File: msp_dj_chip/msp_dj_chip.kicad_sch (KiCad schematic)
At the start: 87 parts, among them J1 Conn_01x04_Pin, J10 Conn_01x02_Socket, J11 Conn_01x02_Socket, J12 Conn_01x02_Socket, J13 Conn_01x02_Socket, J14 Conn_01x02_Socket, J15 Conn_01x02_Socket, J16 Conn_01x02_Socket, J17 Conn_01x02_Socket, J18 Conn_01x02_Socket, J19 Conn_01x02_Socket, J2 Conn_01x04_Pin, J20 Conn_01x02_Socket, J21 Conn_01x02_Socket, J22 Conn_01x06_Socket, J23 Conn_01x06_Socket, J3 Conn_01x02_Socket, J4 Conn_01x02_Socket, J5 Conn_01x02_Socket, J6 Conn_01x02_Socket, J8 Conn_02x05_Odd_Even, J9 Conn_01x02_Socket, SW1 SW_MEC_5E, U2 DAC60502, U4 NCP1117-3.3_SOT223, U8 NCV272DMR2G, Y2 Crystal_GND24_Small

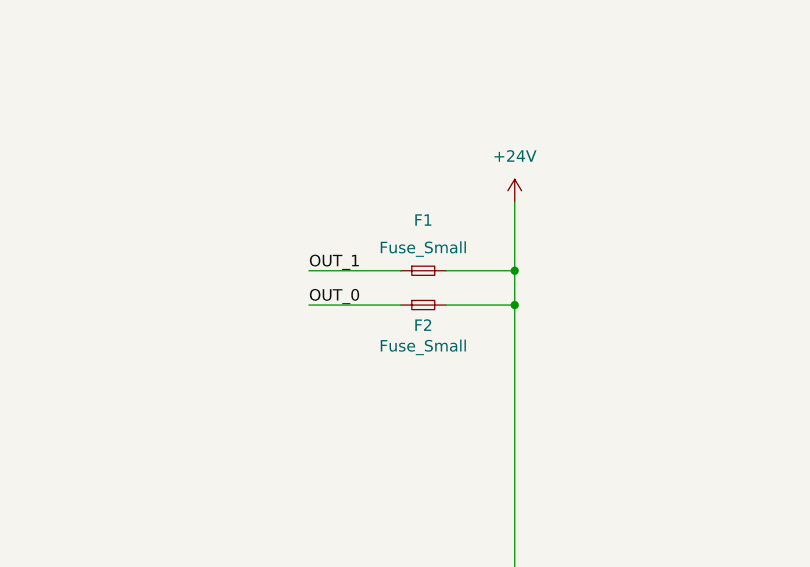
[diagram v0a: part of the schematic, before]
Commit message: Added BAS21W Symbol
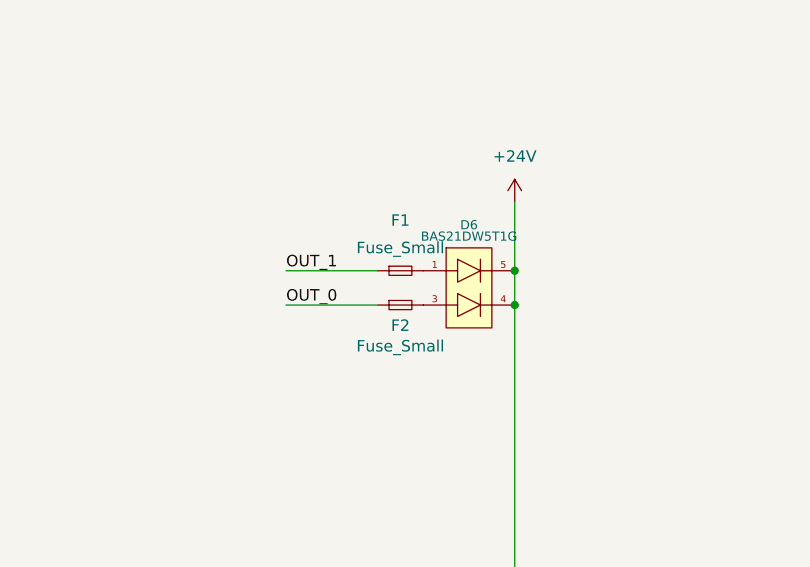
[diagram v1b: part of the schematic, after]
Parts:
- added D6: BAS21DW5T1G, Package_TO_SOT_SMD:SOT-353_SC-70-5, symbol MySymbols:BAS21DW5T1G
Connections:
- net +24V: now also D6.4, D6.5; no longer F1.2, F2.2
- new net: D6.1, F1.2
- new net: D6.3, F2.2
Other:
- moved on the sheet: F1, F2
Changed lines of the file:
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@@
 	)
 	(junction
-		(at 337.82 87.63)
-		(diameter 0)
-		(color 0 0 0 0)
-	)
-	(junction
 		(at 142.24 45.72)
 		(diameter 0)
@@
 	)
 	(junction
-		(at 139.7 255.27)
+		(at 337.82 83.82)
 		(diameter 0)
 		(color 0 0 0 0)
 	)
 	(junction
-		(at 97.79 262.89)
+		(at 139.7 255.27)
 		(diameter 0)
 		(color 0 0 0 0)
 	)
 	(junction
-		(at 105.41 246.38)
+		(at 97.79 262.89)
 		(diameter 0)
 		(color 0 0 0 0)
 	)
 	(junction
-		(at 115.57 40.64)
+		(at 105.41 246.38)
 		(diameter 0)
 		(color 0 0 0 0)
 	)
 	(junction
-		(at 337.82 83.82)
+		(at 115.57 40.64)
 		(diameter 0)
 		(color 0 0 0 0)
@@
 	)
 	(junction
+		(at 337.82 87.63)
+		(diameter 0)
+		(color 0 0 0 0)
+	)
+	(junction
 		(at 175.26 80.01)
 		(diameter 0)
@@
 	(wire
 		(pts
-			(xy 330.2 83.82) (xy 337.82 83.82)
-		)
-		(stroke
-			(width 0)
-			(type default)
-		)
-	)
-	(wire
-		(pts
 			(xy 205.74 124.46) (xy 223.52 124.46)
 		)
@@
 	(wire
 		(pts
-			(xy 330.2 87.63) (xy 337.82 87.63)
-		)
-		(stroke
-			(width 0)
-			(type default)
-		)
-	)
-	(wire
-		(pts
 			(xy 133.35 171.45) (xy 151.13 171.45)
 		)
@@
 	(wire
 		(pts
+			(xy 337.82 87.63) (xy 337.82 199.39)
+		)
+		(stroke
+			(width 0)
+			(type default)
+		)
+	)
+	(wire
+		(pts
 			(xy 105.41 246.38) (xy 105.41 247.65)
 		)
@@
 	(wire
 		(pts
-			(xy 314.96 87.63) (xy 325.12 87.63)
+			(xy 312.42 87.63) (xy 322.58 87.63)
 		)
 		(stroke
@@
 	(wire
 		(pts
-			(xy 337.82 76.2) (xy 337.82 83.82)
-		)
-		(stroke
-			(width 0)
-			(type default)
-		)
-	)
-	(wire
-		(pts
 			(xy 127 264.16) (xy 139.7 264.16)
 		)
@@
 	(wire
 		(pts
-			(xy 337.82 87.63) (xy 337.82 199.39)
-		)
-		(stroke
-			(width 0)
-			(type default)
-		)
-	)
-	(wire
-		(pts
 			(xy 40.64 207.01) (xy 35.56 207.01)
 		)
@@
 	(wire
 		(pts
-			(xy 337.82 83.82) (xy 337.82 87.63)
+			(xy 337.82 76.2) (xy 337.82 83.82)
 		)
 		(stroke
@@
 	(wire
 		(pts
+			(xy 337.82 83.82) (xy 337.82 87.63)
+		)
+		(stroke
+			(width 0)
+			(type default)
+		)
+	)
+	(wire
+		(pts
 			(xy 68.58 39.37) (xy 71.12 39.37)
 		)
@@
 	(wire
 		(pts
-			(xy 314.96 83.82) (xy 325.12 83.82)
+			(xy 312.42 83.82) (xy 322.58 83.82)
 		)
 		(stroke
@@
 	)
 	(label "OUT_0"
-		(at 314.96 87.63 0)
+		(at 312.42 87.63 0)
 		(effects
 			(font
@@
 	)
 	(label "OUT_1"
-		(at 314.96 83.82 0)
+		(at 312.42 83.82 0)
 		(effects
 			(font
@@
 	(symbol
 		(lib_id "Device:Fuse_Small")
-		(at 327.66 83.82 0)
+		(at 325.12 83.82 0)
 		(unit 1)
 		(exclude_from_sim no)
@@
 		(dnp no)
 		(property "Reference" "F1"
-			(at 327.66 78.232 0)
+			(at 325.12 78.232 0)
 			(effects
 				(font
@@
 		)
 		(property "Value" "Fuse_Small"
-			(at 327.66 81.28 0)
+			(at 325.12 81.28 0)
 			(effects
 				(font
@@
 		)
 		(property "Footprint" ""
-			(at 327.66 83.82 0)
+			(at 325.12 83.82 0)
 			(effects
 				(font
@@
 		)
 		(property "Datasheet" "~"
-			(at 327.66 83.82 0)
+			(at 325.12 83.82 0)
 			(effects
 				(font
@@
 		)
 		(property "Description" "Fuse, small symbol"
-			(at 327.66 83.82 0)
+			(at 325.12 83.82 0)
 			(effects
 				(font
@@
 	)
 	(symbol
+		(lib_id "MySymbols:BAS21DW5T1G")
+		(at 331.47 80.01 0)
+		(unit 1)
+		(exclude_from_sim no)
+		(in_bom yes)
+		(on_board yes)
+		(dnp no)
+		(property "Reference" "D6"
+			(at 332.74 78.74 0)
+			(effects
+				(font
+					(size 1.016 1.016)
+				)
+			)
+		)
+		(property "Value" "BAS21DW5T1G"
+			(at 332.74 80.01 0)
+			(effects
+				(font
+					(size 1.016 1.016)
+				)
+			)
+		)
+		(property "Footprint" "Package_TO_SOT_SMD:SOT-353_SC-70-5"
+			(at 331.47 80.01 0)
+			(effects
+				(font
+					(size 1.016 1.016)
+				)
+				(hide yes)
+			)
+		)
+		(property "Datasheet" "https://www.onsemi.com/pdf/datasheet/bas19lt1-d.pdf"
+			(at 331.47 80.01 0)
+			(effects
+				(font
+					(size 1.016 1.016)
+				)
+				(hide yes)
+			)
+		)
+		(property "Description" "DIODE ARRAY GP 250V 200MA SC88A"
+			(at 331.47 80.01 0)
+			(effects
+				(font
+					(size 1.016 1.016)
+				)
+				(hide yes)
+			)
+		)
+		(property "DigiKey Link" "https://www.digikey.com/en/products/detail/onsemi/BAS21DW5T1G/918307"
+			(at 331.47 80.01 0)
+			(effects
+				(font
+					(size 1.016 1.016)
+				)
+				(hide yes)
+			)
+		)
+		(property "LCSC Part" ""
+			(at 331.47 80.01 0)
+			(effects
+				(font
+					(size 1.27 1.27)
+				)
+				(hide yes)
+			)
+		)
+		(property "Manafacture Part #" "BAS21DW5T1G"
+			(at 331.47 80.01 0)
+			(effects
+				(font
+					(size 1.27 1.27)
+				)
+				(hide yes)
+			)
+		)
+		(property "Vendor Link" ""
+			(at 331.47 80.01 0)
+			(effects
+				(font
+					(size 1.27 1.27)
+				)
+				(hide yes)
+			)
+		)
+		(pin "3"
+		)
+		(pin "1"
+		)
+		(pin "5"
+		)
+		(pin "4"
+		)
+		(pin "2"
+		)
+		(instances
+			(project "msp_dj_chip"
+				(path "/9f1d1666-1e71-4846-af68-34a5e483246c"
+					(reference "D6")
+					(unit 1)
+				)
+			)
+		)
+	)
+	(symbol
 		(lib_id "Project_Symbols:DAC_60502")
 		(at 204.47 224.79 0)
@@
 	(symbol
 		(lib_id "Device:Fuse_Small")
-		(at 327.66 87.63 0)
+		(at 325.12 87.63 0)
 		(unit 1)
 		(exclude_from_sim no)
@@
 		(dnp no)
 		(property "Reference" "F2"
-			(at 327.66 89.916 0)
+			(at 325.12 89.916 0)
 			(effects
 				(font
@@
 		)
 		(property "Value" "Fuse_Small"
-			(at 327.66 92.202 0)
+			(at 325.12 92.202 0)
 			(effects
 				(font
@@
 		)
 		(property "Footprint" ""
-			(at 327.66 87.63 0)
+			(at 325.12 87.63 0)
 			(effects
 				(font
@@
 		)
 		(property "Datasheet" "~"
-			(at 327.66 87.63 0)
+			(at 325.12 87.63 0)
 			(effects
 				(font
@@
 		)
 		(property "Description" "Fuse, small symbol"
-			(at 327.66 87.63 0)
+			(at 325.12 87.63 0)
 			(effects
 				(font

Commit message: Update TODO list
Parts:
- removed R27, R28: 1R, symbol Device:R_Small
- added D7, D8: LED_Small_Filled, LED_SMD:LED_0603_1608Metric, symbol Device:LED_Small_Filled
- added R25, R26: 330, symbol Device:R_Small
- added U24: ~, symbol Project_Symbols:mosfet_SSM6N7002KFU
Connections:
- net D is gone; now on net RS485_TX: U1.4 (D)
- net R is gone; now on net RS485_RX: R2.2, U1.1 (R)
- net +3.3V: now also D7.2 (A), D8.2 (A)
- net GND: now also U24.1 (S1), U24.4 (S2)
- net RS485_RX: now also U24.5 (G2)
- net RS485_TX: now also U24.2 (G1)
- net DE renamed RS485_EN_~{RE}
- net RS485_EN_~{RE}: now also U6.1 (PB13)
- net RE renamed RS485_EN_DE
- net RS485_EN_DE: now also U6.2 (PB14)
- removed net RS485_EN: U6.1 (PB13), U6.2 (PB14)
- new net: R25.1, U24. (D2)
- new net: R26.1, U24.6 (D1)
- new net: D7.1 (K), R25.2
- new net: D8.1 (K), R26.2
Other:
- sheet solenoid-driver-boards-dj ports: added SENSE_00; removed none
- note added: "NOT ENOUGH ADC FOR CURR SENSE"
- note added: "VOLTAGE FOLLOWER - OP AMP"
- note removed: "24 Current Sense"
- moved on the sheet: C4, C5, D6, F1, F2, R29, R30, R33, U4, U8A, U8B

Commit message: labeling ERC checking
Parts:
- added D10, D11, D12, D13, D14, D15, D9: BAS21DW5T1G, Package_TO_SOT_SMD:SOT-353_SC-70-5, symbol MySymbols:BAS21DW5T1G
- added F10, F11, F12, F13, F14, F15, F16, F3, F4, F5, F6, F7, F8, F9: Fuse_Small, symbol Device:Fuse_Small
- renumbered C12 to C1, C20 to C10, C4 to C11, C14 to C12, C15 to C13, C13 to C14, C5 to C15, C2 to C16, C3 to C17, C16 to C18, C6 to C2, C7 to C3, C11 to C4, C10 to C5, C9 to C6, C8 to C7, C1 to C8, C21 to C9, D3 to D1, D7 to D2, D8 to D3, D1 to D6, D2 to D7, D6 to D8, J11 to J10, J12 to J11, J13 to J12, J14 to J13, J15 to J14, J16 to J15, J17 to J16, J18 to J17, J19 to J18, J20 to J19, J22 to J2, J21 to J20, J8 to J21, J2 to J22, J23 to J3, J3 to J4, J4 to J5, J5 to J6, J6 to J7, J9 to J8, J10 to J9, R12 to R1, R15 to R10, R16 to R11, R1 to R12, R3 to R13, R2 to R14, R24 to R15, R4 to R16, R5 to R17, R7 to R18, R6 to R19, R19 to R2, R23 to R20, R8 to R21, R9 to R22, R33 to R23, R10 to R24, R11 to R25, R30 to R26, R29 to R27, R21 to R28, R22 to R29, R13 to R3, R20 to R4, R14 to R5, R25 to R6, R26 to R7, R17 to R8, R18 to R9, U24 to U1, U5 to U2, U1 to U3, U6 to U5, U2 to U6, U3 to U7, Y2 to Y1
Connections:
- net +3V3 is gone; now on net +3.3V: J1.3 (Pin_3), R8.1
- net DAC OUT1 is gone; now on net DAC_OUT1: R25.2, U7.7 (OUT_2)
- net NSYNC is gone; now on net SPI_0_CS: R18.2, U6.7 (NSYNC)
- net RSTSEL is gone; now on net GND: U6.3 (RSTSEL)
- net SCLK is gone; now on net SPI_SCLK: U6.6 (SCLK)
- net SDIN is gone; now on net SPI_POCI: U6.8 (SDIN)
- net UART2 RX is gone; now on net FTDI_RX: U2.20 (TXD)
- net UART2 TX is gone; now on net FTDI_TX: U2.4 (RXD)
- net +24V: now also J8.2 (Pin_2), D10.4, D10.5, D11.4, D11.5, D12.4, D12.5, D13.4, D13.5, D14.4, D14.5, D15.4, D15.5, D9.4, D9.5
- net DAC_OUT0: now also R24.2, U7.1 (OUT_1)
- net GND: now also U5.41 (VSS), U6.4 (AGND)
- net OUT_10: now also F11.1
- net OUT_11: now also F12.1
- net OUT_12: now also F13.1
- net OUT_13: now also F14.1
- net OUT_14: now also F15.1
- net OUT_15: now also F16.1
- net OUT_2: now also F3.1
- net OUT_3: now also F4.1
- net OUT_4: now also F5.1
- net OUT_5: now also F6.1
- net OUT_6: now also F7.1
- net OUT_7: now also F8.1
- net OUT_8: now also F9.1
- net OUT_9: now also F10.1
- net SPI_0_CS: now also U5.54 (PA8); no longer U5.42 (PA2)
- net SWCLK: now also J21.4 (Pin_4)
- net SWDIO: now also J21.2 (Pin_2)
- net USB_D+: now also C3.1, R1.1
- net USB_D-: now also C2.1, R3.1
- net nRESET: now also R5.2
- net ROSC: now reaches R15.2
- net ROSC: now also U5.42 (PA2)
- net ADC_SOL_0 renamed ADC_SOL_00
- net ADC_SOL_1 renamed ADC_SOL_01
- net ADC_SOL_2 renamed ADC_SOL_02
- net ADC_SOL_3 renamed ADC_SOL_03
- net ADC_SOL_4 renamed ADC_SOL_04
- net ADC_SOL_5 renamed ADC_SOL_05
- net ADC_SOL_6 renamed ADC_SOL_06
- net ADC_SOL_7 renamed ADC_SOL_07
- net ADC_SOL_8 renamed ADC_SOL_08
- net ADC_SOL_9 renamed ADC_SOL_09
- net DAC OUT0: no longer names the net of R26.2, R27.2, U8.1 (OUT_1)
- net DAC OUT0: no longer R24.2, U7.1 (OUT_1)
- net DAC_0 renamed DAC_00
- new net: D11.1, F7.2
- new net: D9.3, F4.2
- new net: D14.1, F13.2
- new net: D14.3, F14.2
- new net: D10.1, F5.2
- new net: D10.3, F6.2
- new net: D9.1, F3.2
- new net: D15.1, F15.2
- new net: D12.1, F9.2
- new net: D12.3, F10.2
- new net: D15.3, F16.2
- new net: D11.3, F8.2
- new net: D13.1, F11.2
- new net: D13.3, F12.2
- no-connect marks 13 -> 28
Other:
- sheet solenoid-driver-boards-dj ports: added GPIO_INPUT_02, GPIO_INPUT_03, GPIO_INPUT_04, GPIO_INPUT_05, GPIO_INPUT_06, GPIO_INPUT_07, GPIO_INPUT_08, GPIO_INPUT_09, GPIO_INPUT_10, GPIO_INPUT_11, GPIO_INPUT_12, GPIO_INPUT_13, GPIO_INPUT_14, GPIO_INPUT_15, OUT_02, OUT_03, OUT_04, OUT_05, OUT_06, OUT_07, OUT_08, OUT_09, OUT_10, OUT_11, OUT_12, OUT_13, OUT_14, OUT_15, SENSE_01, SENSE_02, SENSE_03, SENSE_04, SENSE_05, SENSE_06, SENSE_07, SENSE_08, SENSE_09, SENSE_10, SENSE_11, SENSE_12, SENSE_13, SENSE_14, SENSE_15; removed none
- note added: "+_0.1% +-25PPM"
- note added: "NOT ENOUGH ADCS"
- moved on the sheet: D8, F1, F2, R15, R23

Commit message: cleanup changes
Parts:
- added unit 2 of U7
- D10, D11, D12, D13, D14, D15, D8, D9: symbol MySymbols:BAS21DW5T1G -> Project_Symbols:BAS21DW5T1G
- U7: value ~ -> NCV272DMR2G; Digikey Link (none) -> https://www.digikey.com/en/products/detail/onsemi/NCV272DMR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
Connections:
- net +24V: now also U7.8 (VDD); no longer U7.8 (VDD)
- net DAC_OUT0: now also U7.7 (OUT_2); no longer U7.1 (OUT_1)
- net DAC_OUT1: now also U7.1 (OUT_1); no longer U7.7 (OUT_2)
- net GND: now also U7.4 (VSS); no longer U7.4 (VSS)
- net VOUTA: now also U7.5 (IN+2); no longer U7.3 (IN+1)
- net VOUTB: now also U7.3 (IN+1); no longer U7.5 (IN+2)
- net at R21.2, R24.1: now also U7.6 (IN-2); no longer U7.2 (IN-1)
- net at R22.2, R25.1: now also U7.2 (IN-1); no longer U7.6 (IN-2)
- net +3.3V renamed +3V3
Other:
- note added: "SWD HEADER"
- note removed: "PROGRAMMING HEADER"
- moved on the sheet: C10, C11, C12, C13, C14, C15, C18, C8, C9, J10, J11, J12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

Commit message: updating footprint assignments
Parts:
- C1, C2, C3, C5, C6, C7, C8: footprint Capacitor_SMD:C_0402_1005Metric -> Capacitor_SMD:C_0603_1608Metric
- C10, C12, C13, C14, C18, C4, C9, F1, F10, F11, F12, F13, F14, F15, F16, F2, F3, F4, F5, F6, F7, F8, F9: footprint (none) -> Capacitor_SMD:C_0603_1608Metric
- R1, R10, R11, R12, R13, R14, R15, R16, R17, R18, R19, R2, R20, R21, R22, R23, R24, R25, R26, R27, R28, R29, R3, R4, R5, R6, R7, R8, R9: footprint (none) -> Resistor_SMD:R_0603_1608Metric
- TP1: footprint (none) -> TestPoint:TestPoint_Pad_2.0x2.0mm
- U1, U2, U5: value ~ -> SSM6N7002KFU
- U3: value ~ -> THVD2442; footprint (none) -> project_footprints:RS_485_THVD24
- U6: footprint (none) -> project_footprints:DAC60502
- U7, U8: footprint (none) -> Package_SO:MSOP-8_3x3mm_P0.65mm

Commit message: more footprint assignments
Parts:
- J1: footprint (none) -> TerminalBlock_Phoenix:TerminalBlock_Phoenix_MKDS-1,5-4-5.08_1x04_P5.08mm_Horizontal
- J10, J11, J12, J13, J14, J15, J16, J17, J18, J19, J20, J4, J5, J6, J7, J8, J9: footprint (none) -> project_footprints:PPPC021LFBN-RC
- J2, J3: footprint (none) -> project_footprints:CONN HEADER RA 6POS 2MM
- J21: footprint (none) -> project_footprints:CONN HEADER VERT 10POS 1.27MM
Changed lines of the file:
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@@
 			)
 		)
-		(property "Footprint" ""
+		(property "Footprint" "project_footprints:PPPC021LFBN-RC"
 			(at 375.92 186.69 0)
 			(effects
@@
 			)
 		)
-		(property "Footprint" ""
+		(property "Footprint" "project_footprints:PPPC021LFBN-RC"
 			(at 375.92 143.51 0)
 			(effects
@@
 			)
 		)
-		(property "Footprint" ""
+		(property "Footprint" "project_footprints:CONN HEADER VERT 10POS 1.27MM"
 			(at 379.73 220.98 0)
 			(effects
@@
 			)
 		)
-		(property "Footprint" ""
+		(property "Footprint" "project_footprints:PPPC021LFBN-RC"
 			(at 375.92 135.89 0)
 			(effects
@@
 			)
 		)
-		(property "Footprint" ""
+		(property "Footprint" "project_footprints:PPPC021LFBN-RC"
 			(at 375.92 81.28 0)
 			(effects
@@
 			)
 		)
-		(property "Footprint" ""
+		(property "Footprint" "project_footprints:PPPC021LFBN-RC"
 			(at 375.92 128.27 0)
 			(effects
@@
 			)
 		)
-		(property "Footprint" ""
+		(property "Footprint" "project_footprints:PPPC021LFBN-RC"
 			(at 375.92 74.93 0)
 			(effects
@@
 			)
 		)
-		(property "Footprint" ""
+		(property "Footprint" "TerminalBlock_Phoenix:TerminalBlock_Phoenix_MKDS-1,5-4-5.08_1x04_P5.08mm_Horizontal"
 			(at 21.59 41.91 0)
 			(effects
@@
 			)
 		)
-		(property "Footprint" ""
+		(property "Footprint" "project_footprints:PPPC021LFBN-RC"
 			(at 375.92 106.68 0)
 			(effects
@@
 			)
 		)
-		(property "Footprint" ""
+		(property "Footprint" "project_footprints:PPPC021LFBN-RC"
 			(at 375.92 113.03 0)
 			(effects
@@
 			)
 		)
-		(property "Footprint" ""
+		(property "Footprint" "project_footprints:PPPC021LFBN-RC"
 			(at 375.92 100.33 0)
 			(effects
@@
 		(exclude_from_sim no)
 		(in_bom yes)
-		(on_board yes)
+		(on_board no)
 		(dnp no)
 		(property "Reference" "J3"
@@
 			)
 		)
-		(property "Footprint" ""
+		(property "Footprint" "project_footprints:CONN HEADER RA 6POS 2MM"
 			(at 365.76 242.57 0)
 			(effects
@@
 			)
 		)
-		(property "Footprint" ""
+		(property "Footprint" "project_footprints:PPPC021LFBN-RC"
 			(at 375.92 87.63 0)
 			(effects
@@
 			)
 		)
-		(property "Footprint" ""
+		(property "Footprint" "project_footprints:PPPC021LFBN-RC"
 			(at 375.92 151.13 0)
 			(effects
@@
 			)
 		)
-		(property "Footprint" ""
+		(property "Footprint" "project_footprints:PPPC021LFBN-RC"
 			(at 375.92 179.07 0)
 			(effects
@@
 			)
 		)
-		(property "Footprint" ""
+		(property "Footprint" "project_footprints:PPPC021LFBN-RC"
 			(at 375.92 93.98 0)
 			(effects
@@
 			)
 		)
-		(property "Footprint" ""
+		(property "Footprint" "project_footprints:PPPC021LFBN-RC"
 			(at 375.92 166.37 0)
 			(effects
@@
 		(exclude_from_sim no)
 		(in_bom yes)
-		(on_board yes)
+		(on_board no)
 		(dnp no)
 		(property "Reference" "J2"
@@
 			)
 		)
-		(property "Footprint" ""
+		(property "Footprint" "project_footprints:CONN HEADER RA 6POS 2MM"
 			(at 24.13 74.93 0)
 			(effects
@@
 			)
 		)
-		(property "Footprint" ""
+		(property "Footprint" "project_footprints:PPPC021LFBN-RC"
 			(at 375.92 158.75 0)
 			(effects
@@
 			)
 		)
-		(property "Footprint" ""
+		(property "Footprint" "project_footprints:PPPC021LFBN-RC"
 			(at 375.92 172.72 0)
 			(effects
@@
 			)
 		)
-		(property "Footprint" ""
+		(property "Footprint" "project_footprints:PPPC021LFBN-RC"
 			(at 375.92 120.65 0)
 			(effects

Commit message: mosfet footprint assignments
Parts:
- U1, U2, U5: footprint (none) -> project_footprints:MOSFET SSM6N7002KFU
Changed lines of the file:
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@@
 			)
 		)
-		(property "Footprint" ""
+		(property "Footprint" "project_footprints:MOSFET SSM6N7002KFU"
 			(at 44.45 260.35 0)
 			(effects
@@
 			)
 		)
-		(property "Footprint" ""
+		(property "Footprint" "project_footprints:MOSFET SSM6N7002KFU"
 			(at 64.77 123.19 0)
 			(effects
@@
 			)
 		)
-		(property "Footprint" ""
+		(property "Footprint" "project_footprints:MOSFET SSM6N7002KFU"
 			(at 171.45 119.38 0)
 			(effects

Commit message: mark changes
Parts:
- removed R23: 1K, Resistor_SMD:R_0603_1608Metric, symbol Device:R_Small
- removed R26, R27: 2K2, Resistor_SMD:R_0603_1608Metric, symbol Device:R_Small
- added TP83: Vcore TP, symbol Connector:TestPoint
- U2: value SSM6N7002KFU -> FT231XS-R
- Y1: value Crystal_GND24_Small -> 24 MHz
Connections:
- net ADC_SOL_10: now also U8.3 (IN+1); no longer U5.9 (PA16)
- net ADC_SOL_10_BUF: now reaches U8.1 (OUT_1)
- net ADC_SOL_10_BUF: now also U5.9 (PA16), U8.2 (IN-1)
- net at C13.1, U5.32 (VCORE): now also TP83.1
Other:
- note added: "* TODO Make all sheet to sheet global labels"
- note added: "*TODO Put in Crystal part #"
- note added: "*TODO RESET NOT CONFIGURED CORRECTLY"
- note added: "Vcore should +1.35 VDC"
- moved on the sheet: C10, C12, C14, U8A, U8B
